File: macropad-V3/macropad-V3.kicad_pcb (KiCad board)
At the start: 2 copper layers, 136.5 x 56.4 mm, 12 parts, among them SW1 SW_Push, U1 ARDUINO_PRO_MICRO

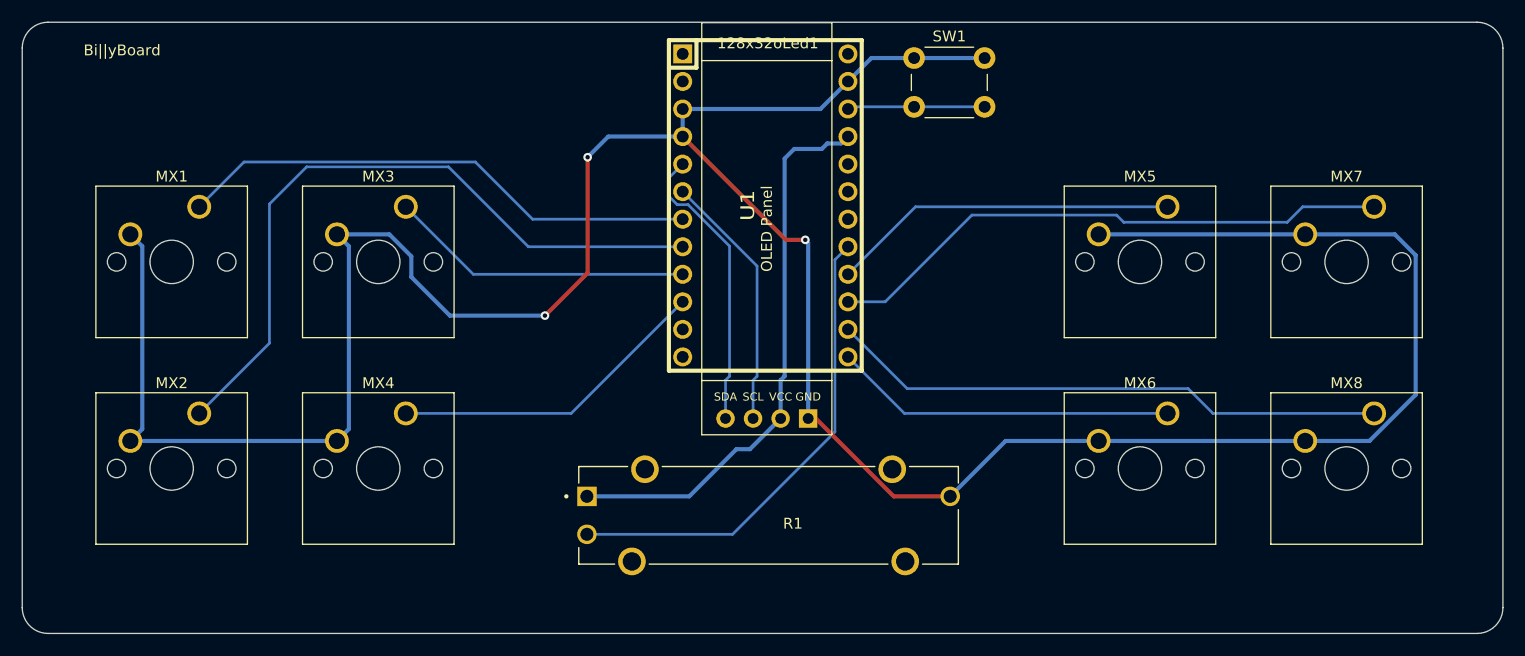
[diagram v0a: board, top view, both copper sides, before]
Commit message: added pull up resistors/added ground plane/routed traces
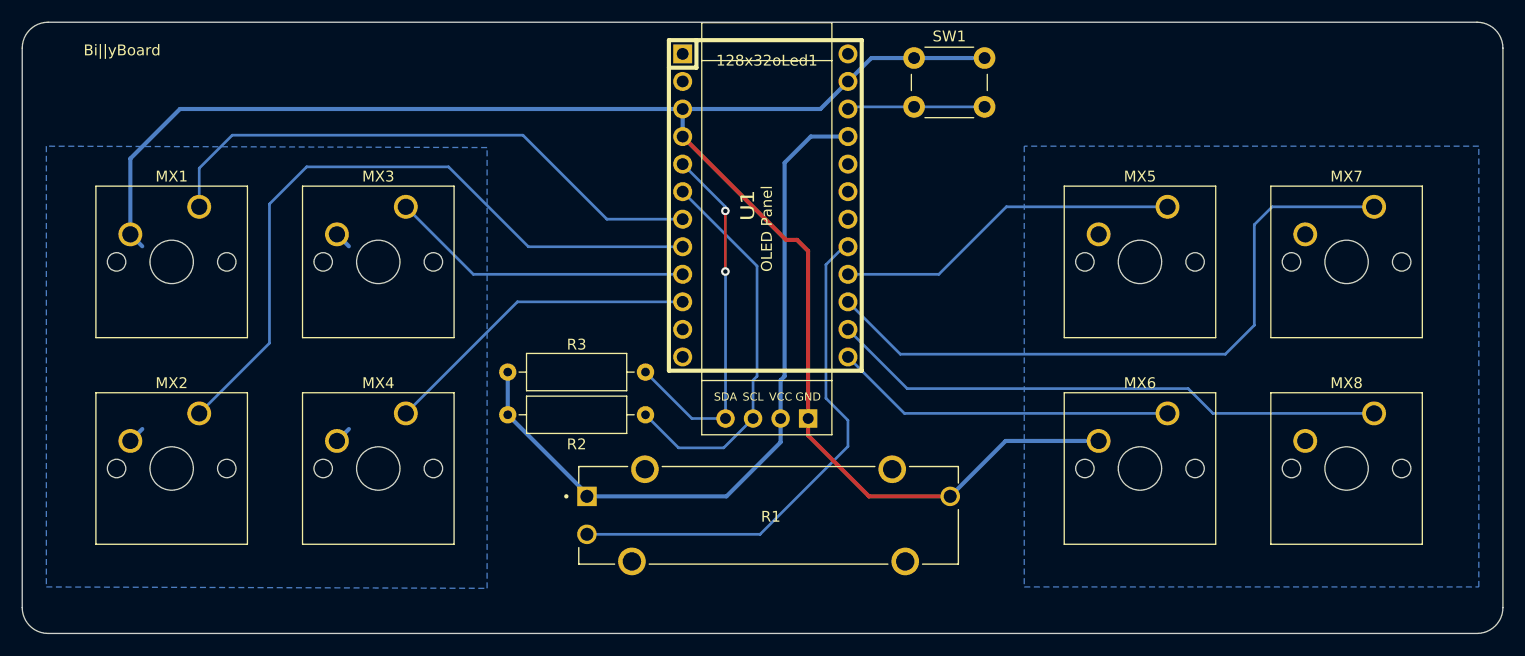
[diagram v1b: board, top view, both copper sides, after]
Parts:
- added R2: 4.7k, Resistor_THT:R_Axial_DIN0309_L9.0mm_D3.2mm_P12.70mm_Horizontal, F.Cu at (128.9, 87.0)
- added R3: 4.7k, Resistor_THT:R_Axial_DIN0309_L9.0mm_D3.2mm_P12.70mm_Horizontal, F.Cu at (128.9, 83.1)
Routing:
- net GND: track 278.4 -> 162.9 mm, vias 3 -> 0
- net VCC: track 51.6 -> 67.2 mm
- net SCL: track 23.9 -> 36.2 mm
- net KEY6: track 54.2 -> 63.1 mm
- net SDA: track 27.0 -> 34.2 mm, vias 0 -> 2
- net KEY0: track 49.2 -> 53.3 mm
- net ADC0: track 44.4 -> 48.1 mm
- added copper zone on B.Cu, net GND

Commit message: updated routing
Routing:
- net GND: track 162.9 -> 162.3 mm
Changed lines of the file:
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@@
   (segment (start 143.903 88.912) (end 143.903 87.338) (width 0.381) (layer "F.Cu") (net 3))
   (segment (start 157.0035 94.516) (end 149.507 94.516) (width 0.381) (layer "F.Cu") (net 3))
-  (segment (start 143.903 87.338) (end 143.903 71.894) (width 0.381) (layer "F.Cu") (net 3))
-  (segment (start 132.334 61.341) (end 141.859 70.866) (width 0.381) (layer "F.Cu") (net 3))
+  (segment (start 143.903 87.338) (end 143.903 72.91) (width 0.381) (layer "F.Cu") (net 3))
   (segment (start 149.507 94.516) (end 143.903 88.912) (width 0.381) (layer "F.Cu") (net 3))
-  (segment (start 141.859 70.866) (end 142.875 70.866) (width 0.381) (layer "F.Cu") (net 3))
-  (segment (start 143.903 71.894) (end 142.875 70.866) (width 0.381) (layer "F.Cu") (net 3))
+  (segment (start 143.903 72.91) (end 132.334 61.341) (width 0.381) (layer "F.Cu") (net 3))
   (segment (start 85.979 58.801) (end 132.334 58.801) (width 0.381) (layer "B.Cu") (net 3))
   (segment (start 149.733 54.102) (end 147.574 56.261) (width 0.381) (layer "B.Cu") (net 3))
@@
   (segment (start 141.363 89.523) (end 141.363 87.338) (width 0.381) (layer "B.Cu") (net 4))
   (segment (start 116.205 83.058) (end 116.205 86.995) (width 0.381) (layer "B.Cu") (net 4))
-  (segment (start 141.363 87.338) (end 141.363 83.808) (width 0.381) (layer "B.Cu") (net 4))
   (segment (start 136.37 94.516) (end 141.363 89.523) (width 0.381) (layer "B.Cu") (net 4))
   (segment (start 123.5035 94.2935) (end 123.5035 94.516) (width 0.381) (layer "B.Cu") (net 4))
-  (segment (start 144.145 61.341) (end 141.732 63.754) (width 0.381) (layer "B.Cu") (net 4))
+  (segment (start 141.363 64.123) (end 144.145 61.341) (width 0.381) (layer "B.Cu") (net 4))
   (segment (start 116.205 86.995) (end 123.5035 94.2935) (width 0.381) (layer "B.Cu") (net 4))
-  (segment (start 141.363 83.808) (end 141.732 83.439) (width 0.381) (layer "B.Cu") (net 4))
-  (segment (start 141.732 83.439) (end 141.732 63.754) (width 0.381) (layer "B.Cu") (net 4))
   (segment (start 123.5035 94.516) (end 136.37 94.516) (width 0.381) (layer "B.Cu") (net 4))
-  (segment (start 147.574 61.341) (end 144.145 61.341) (width 0.381) (layer "B.Cu") (net 4))
-  (segment (start 139.192 83.439) (end 139.192 73.279) (width 0.25) (layer "B.Cu") (net 5))
-  (segment (start 138.823 87.338) (end 138.823 83.808) (width 0.25) (layer "B.Cu") (net 5))
+  (segment (start 141.363 87.338) (end 141.363 64.123) (width 0.381) (layer "B.Cu") (net 4))
+  (segment (start 144.145 61.341) (end 147.574 61.341) (width 0.381) (layer "B.Cu") (net 4))
   (segment (start 131.953 90.043) (end 128.905 86.995) (width 0.25) (layer "B.Cu") (net 5))
   (segment (start 138.823 87.338) (end 136.118 90.043) (width 0.25) (layer "B.Cu") (net 5))
-  (segment (start 138.823 83.808) (end 139.192 83.439) (width 0.25) (layer "B.Cu") (net 5))
-  (segment (start 139.192 73.279) (end 132.334 66.421) (width 0.25) (layer "B.Cu") (net 5))
+  (segment (start 138.823 72.91) (end 132.334 66.421) (width 0.25) (layer "B.Cu") (net 5))
   (segment (start 136.118 90.043) (end 131.953 90.043) (width 0.25) (layer "B.Cu") (net 5))
+  (segment (start 138.823 87.338) (end 138.823 72.91) (width 0.25) (layer "B.Cu") (net 5))
   (segment (start 136.271 73.787) (end 136.271 68.199) (width 0.25) (layer "F.Cu") (net 6))
   (via (at 136.271 73.787) (size 0.8) (drill 0.4) (layers "F.Cu" "B.Cu") (net 6))
